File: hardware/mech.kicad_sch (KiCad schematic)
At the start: 16 parts

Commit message: usb, charger, sensors, heir
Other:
- company: (none) -> Frisius
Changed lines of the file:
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@@
 (kicad_sch (version 20211123) (generator eeschema)
-  (paper "A5")
+  (paper "A4")
+  (title_block
+    (company "Frisius")
+  )
   (wire (pts (xy 104.14 45.72) (xy 104.14 44.45))
     (stroke (width 0) (type default) (color 0 0 0 0))

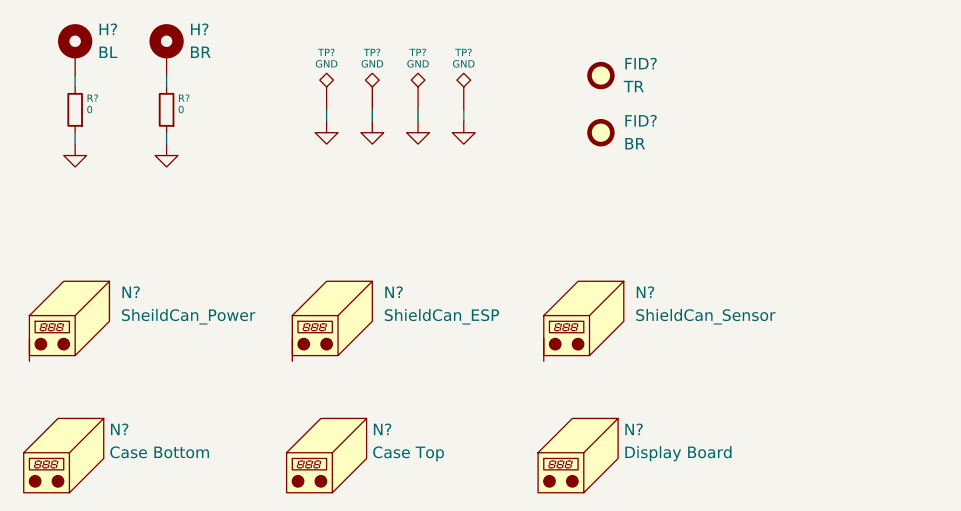
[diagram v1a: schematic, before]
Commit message: checking footprint assignment, added current sense pac1934 for dev
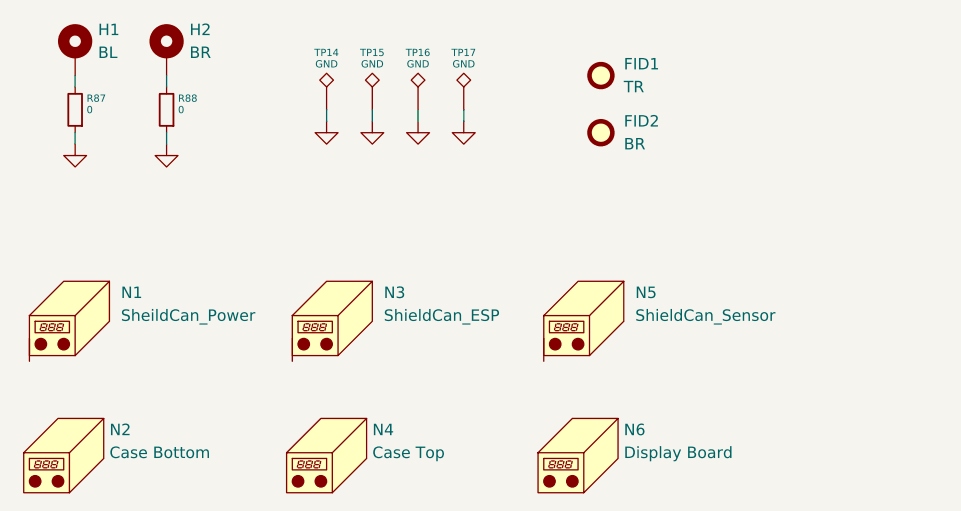
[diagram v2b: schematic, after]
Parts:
- FID1, FID2: renamed from FID?; footprint (none) -> Fiducial:Fiducial_0.5mm_Mask1.5mm
- gave numbers to parts that had none: 14
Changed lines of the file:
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@@
   (symbol (lib_id "power:GND") (at 104.14 45.72 0) (unit 1)
     (in_bom yes) (on_board yes) (fields_autoplaced)
-    (property "Reference" "#PWR?" (id 0) (at 104.14 52.07 0)
+    (property "Reference" "#PWR074" (id 0) (at 104.14 52.07 0)
       (effects (font (size 0.8 0.8)) hide)
     )
@@
   (symbol (lib_id "Mechanical:Housing") (at 128.27 82.55 0) (unit 1)
     (in_bom yes) (on_board yes)
-    (property "Reference" "N?" (id 0) (at 132.08 80.01 0)
+    (property "Reference" "N6" (id 0) (at 132.08 80.01 0)
       (effects (font (size 1.27 1.27)) (justify left))
     )
@@
   (symbol (lib_id "Connector:TestPoint_Alt") (at 114.3 44.45 0) (unit 1)
     (in_bom yes) (on_board yes)
-    (property "Reference" "TP?" (id 0) (at 114.3 38.1 0)
+    (property "Reference" "TP17" (id 0) (at 114.3 38.1 0)
       (effects (font (size 0.8 0.8)))
     )
@@
   (symbol (lib_id "Device:R_Small") (at 81.28 44.45 180) (unit 1)
     (in_bom yes) (on_board yes)
-    (property "Reference" "R?" (id 0) (at 82.55 43.18 0)
+    (property "Reference" "R88" (id 0) (at 82.55 43.18 0)
       (effects (font (size 0.8 0.8)) (justify right))
     )
@@
   (symbol (lib_id "Mechanical:Housing") (at 71.12 82.55 0) (unit 1)
     (in_bom yes) (on_board yes)
-    (property "Reference" "N?" (id 0) (at 74.93 80.01 0)
+    (property "Reference" "N2" (id 0) (at 74.93 80.01 0)
       (effects (font (size 1.27 1.27)) (justify left))
     )
@@
   (symbol (lib_id "power:GND") (at 109.22 45.72 0) (unit 1)
     (in_bom yes) (on_board yes) (fields_autoplaced)
-    (property "Reference" "#PWR?" (id 0) (at 109.22 52.07 0)
+    (property "Reference" "#PWR075" (id 0) (at 109.22 52.07 0)
       (effects (font (size 0.8 0.8)) hide)
     )
@@
   (symbol (lib_id "power:GND") (at 99.06 45.72 0) (unit 1)
     (in_bom yes) (on_board yes) (fields_autoplaced)
-    (property "Reference" "#PWR?" (id 0) (at 99.06 52.07 0)
+    (property "Reference" "#PWR073" (id 0) (at 99.06 52.07 0)
       (effects (font (size 0.8 0.8)) hide)
     )
@@
   (symbol (lib_id "Mechanical:Fiducial") (at 129.54 40.64 0) (unit 1)
     (in_bom yes) (on_board yes) (fields_autoplaced)
-    (property "Reference" "FID?" (id 0) (at 132.08 39.3699 0)
+    (property "Reference" "FID1" (id 0) (at 132.08 39.3699 0)
       (effects (font (size 1.27 1.27)) (justify left))
     )
@@
       (effects (font (size 1.27 1.27)) (justify left))
     )
-    (property "Footprint" "" (id 2) (at 129.54 40.64 0)
+    (property "Footprint" "Fiducial:Fiducial_0.5mm_Mask1.5mm" (id 2) (at 129.54 40.64 0)
       (effects (font (size 1.27 1.27)) hide)
     )
@@
   (symbol (lib_id "Mechanical:Housing_Pad") (at 128.27 67.31 0) (unit 1)
     (in_bom yes) (on_board yes)
-    (property "Reference" "N?" (id 0) (at 133.35 64.77 0)
+    (property "Reference" "N5" (id 0) (at 133.35 64.77 0)
       (effects (font (size 1.27 1.27)) (justify left))
     )
@@
   (symbol (lib_id "Mechanical:Housing") (at 100.33 82.55 0) (unit 1)
     (in_bom yes) (on_board yes)
-    (property "Reference" "N?" (id 0) (at 104.14 80.01 0)
+    (property "Reference" "N4" (id 0) (at 104.14 80.01 0)
       (effects (font (size 1.27 1.27)) (justify left))
     )
@@
   (symbol (lib_id "Mechanical:Housing_Pad") (at 100.33 67.31 0) (unit 1)
     (in_bom yes) (on_board yes)
-    (property "Reference" "N?" (id 0) (at 105.41 64.77 0)
+    (property "Reference" "N3" (id 0) (at 105.41 64.77 0)
       (effects (font (size 1.27 1.27)) (justify left))
     )
@@
   (symbol (lib_id "power:GND") (at 81.28 48.26 0) (unit 1)
     (in_bom yes) (on_board yes) (fields_autoplaced)
-    (property "Reference" "#PWR?" (id 0) (at 81.28 54.61 0)
+    (property "Reference" "#PWR072" (id 0) (at 81.28 54.61 0)
       (effects (font (size 0.8 0.8)) hide)
     )
@@
   (symbol (lib_id "Connector:TestPoint_Alt") (at 104.14 44.45 0) (unit 1)
     (in_bom yes) (on_board yes)
-    (property "Reference" "TP?" (id 0) (at 104.14 38.1 0)
+    (property "Reference" "TP15" (id 0) (at 104.14 38.1 0)
       (effects (font (size 0.8 0.8)))
     )
@@
   (symbol (lib_id "power:GND") (at 71.12 48.26 0) (unit 1)
     (in_bom yes) (on_board yes) (fields_autoplaced)
-    (property "Reference" "#PWR?" (id 0) (at 71.12 54.61 0)
+    (property "Reference" "#PWR071" (id 0) (at 71.12 54.61 0)
       (effects (font (size 0.8 0.8)) hide)
     )
@@
   (symbol (lib_id "Mechanical:Housing_Pad") (at 71.12 67.31 0) (unit 1)
     (in_bom yes) (on_board yes)
-    (property "Reference" "N?" (id 0) (at 76.2 64.77 0)
+    (property "Reference" "N1" (id 0) (at 76.2 64.77 0)
       (effects (font (size 1.27 1.27)) (justify left))
     )
@@
   (symbol (lib_id "Mechanical:MountingHole_Pad") (at 81.28 38.1 0) (unit 1)
     (in_bom yes) (on_board yes) (fields_autoplaced)
-    (property "Reference" "H?" (id 0) (at 83.82 35.5599 0)
+    (property "Reference" "H2" (id 0) (at 83.82 35.5599 0)
       (effects (font (size 1.27 1.27)) (justify left))
     )
@@
   (symbol (lib_id "Mechanical:MountingHole_Pad") (at 71.12 38.1 0) (unit 1)
     (in_bom yes) (on_board yes) (fields_autoplaced)
-    (property "Reference" "H?" (id 0) (at 73.66 35.5599 0)
+    (property "Reference" "H1" (id 0) (at 73.66 35.5599 0)
       (effects (font (size 1.27 1.27)) (justify left))
     )
@@
   (symbol (lib_id "power:GND") (at 114.3 45.72 0) (unit 1)
     (in_bom yes) (on_board yes) (fields_autoplaced)
-    (property "Reference" "#PWR?" (id 0) (at 114.3 52.07 0)
+    (property "Reference" "#PWR076" (id 0) (at 114.3 52.07 0)
       (effects (font (size 0.8 0.8)) hide)
     )
@@
   (symbol (lib_id "Connector:TestPoint_Alt") (at 99.06 44.45 0) (unit 1)
     (in_bom yes) (on_board yes)
-    (property "Reference" "TP?" (id 0) (at 99.06 38.1 0)
+    (property "Reference" "TP14" (id 0) (at 99.06 38.1 0)
       (effects (font (size 0.8 0.8)))
     )
@@
   (symbol (lib_id "Device:R_Small") (at 71.12 44.45 180) (unit 1)
     (in_bom yes) (on_board yes)
-    (property "Reference" "R?" (id 0) (at 72.39 43.18 0)
+    (property "Reference" "R87" (id 0) (at 72.39 43.18 0)
       (effects (font (size 0.8 0.8)) (justify right))
     )
@@
   (symbol (lib_id "Mechanical:Fiducial") (at 129.54 46.99 0) (unit 1)
     (in_bom yes) (on_board yes) (fields_autoplaced)
-    (property "Reference" "FID?" (id 0) (at 132.08 45.7199 0)
+    (property "Reference" "FID2" (id 0) (at 132.08 45.7199 0)
       (effects (font (size 1.27 1.27)) (justify left))
     )
@@
       (effects (font (size 1.27 1.27)) (justify left))
     )
-    (property "Footprint" "" (id 2) (at 129.54 46.99 0)
+    (property "Footprint" "Fiducial:Fiducial_0.5mm_Mask1.5mm" (id 2) (at 129.54 46.99 0)
       (effects (font (size 1.27 1.27)) hide)
     )
@@
   (symbol (lib_id "Connector:TestPoint_Alt") (at 109.22 44.45 0) (unit 1)
     (in_bom yes) (on_board yes)
-    (property "Reference" "TP?" (id 0) (at 109.22 38.1 0)
-      (effects (font (size 0.8 0.8)))
-    )
+    (property "Reference" "TP16" (id 0) (at 109.22 38.1 0)
+      (effects (font (size 0.8 0.8)))
+    )

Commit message: hardware update
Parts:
- removed FID1: TR, Fiducial:Fiducial_0.5mm_Mask1.5mm, symbol Mechanical:Fiducial
- removed FID2: BR, Fiducial:Fiducial_0.5mm_Mask1.5mm, symbol Mechanical:Fiducial
- removed R87, R88: 0, Resistor_SMD:R_0603_1608Metric, symbol Device:R_Small
- removed TP14, TP15, TP16, TP17: GND, TestPoint:TestPoint_Keystone_5015_Micro-Minature, symbol Connector:TestPoint_Alt
- added N7: Battery, symbol Mechanical:Housing
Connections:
- net GND: now also H1.1, H2.1
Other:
- moved on the sheet: H1, H2

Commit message: schematic tidy up, component placement, shielding investigation
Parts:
- removed N5: ShieldCan_Sensor, symbol Mechanical:Housing_Pad
- N3: footprint (none) -> RF_Shielding:Laird_Technologies_BMI-S-102_16.50x16.50mm
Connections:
- net GND: now also N3.1 (PAD)
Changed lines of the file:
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@@
+    (stroke (width 0) (type default) (color 0 0 0 0))
+  )
+  (wire (pts (xy 95.25 73.66) (xy 95.25 72.39))
     (stroke (width 0) (type default) (color 0 0 0 0))
   )
@@
     )
   )
+  (symbol (lib_id "power:GND") (at 95.25 73.66 0) (unit 1)
+    (in_bom yes) (on_board yes) (fields_autoplaced)
+    (property "Reference" "#PWR?" (id 0) (at 95.25 80.01 0)
+      (effects (font (size 0.8 0.8)) hide)
+    )
+    (property "Value" "GND" (id 1) (at 95.25 78.74 0)
+      (effects (font (size 0.8 0.8)) hide)
+    )
+    (property "Footprint" "" (id 2) (at 95.25 73.66 0)
+      (effects (font (size 0.8 0.8)) hide)
+    )
+    (property "Datasheet" "" (id 3) (at 95.25 73.66 0)
+      (effects (font (size 0.8 0.8)) hide)
+    )
+    (pin "1")
+  )
   (symbol (lib_id "Mechanical:Housing") (at 154.94 82.55 0) (unit 1)
     (in_bom yes) (on_board yes)
@@
       (effects (font (size 1.27 1.27)) hide)
     )
-  )
-  (symbol (lib_id "Mechanical:Housing_Pad") (at 128.27 67.31 0) (unit 1)
-    (in_bom yes) (on_board yes)
-    (property "Reference" "N5" (id 0) (at 133.35 64.77 0)
-      (effects (font (size 1.27 1.27)) (justify left))
-    )
-    (property "Value" "ShieldCan_Sensor" (id 1) (at 133.35 67.31 0)
-      (effects (font (size 1.27 1.27)) (justify left))
-    )
-    (property "Footprint" "" (id 2) (at 130.175 66.04 0)
-      (effects (font (size 1.27 1.27)) hide)
-    )
-    (property "Datasheet" "~" (id 3) (at 130.175 66.04 0)
-      (effects (font (size 1.27 1.27)) hide)
-    )
-    (pin "1")
   )
   (symbol (lib_id "Mechanical:Housing") (at 100.33 82.55 0) (unit 1)
@@
       (effects (font (size 1.27 1.27)) (justify left))
     )
-    (property "Footprint" "" (id 2) (at 102.235 66.04 0)
+    (property "Footprint" "RF_Shielding:Laird_Technologies_BMI-S-102_16.50x16.50mm" (id 2) (at 102.235 66.04 0)
       (effects (font (size 1.27 1.27)) hide)
     )

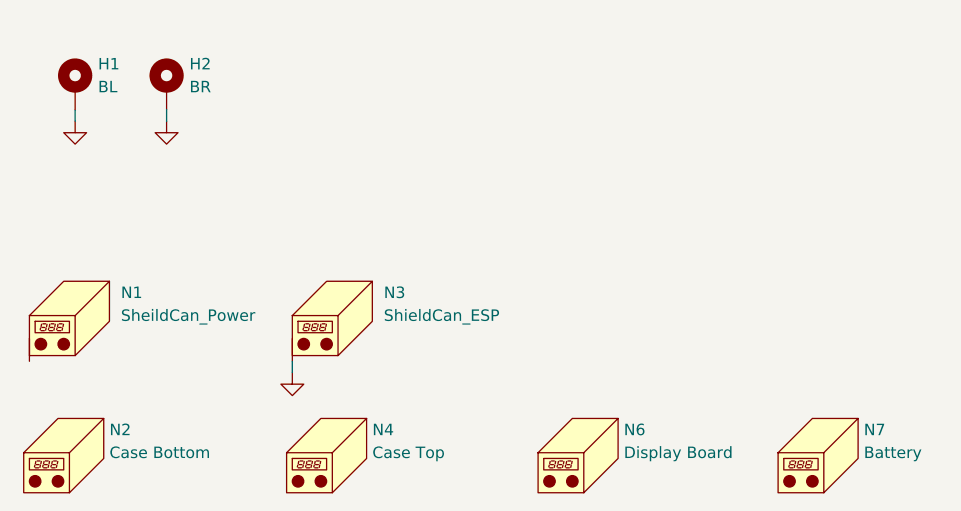
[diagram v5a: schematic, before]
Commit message: minor sch tweaks, more layout, added power emc shield
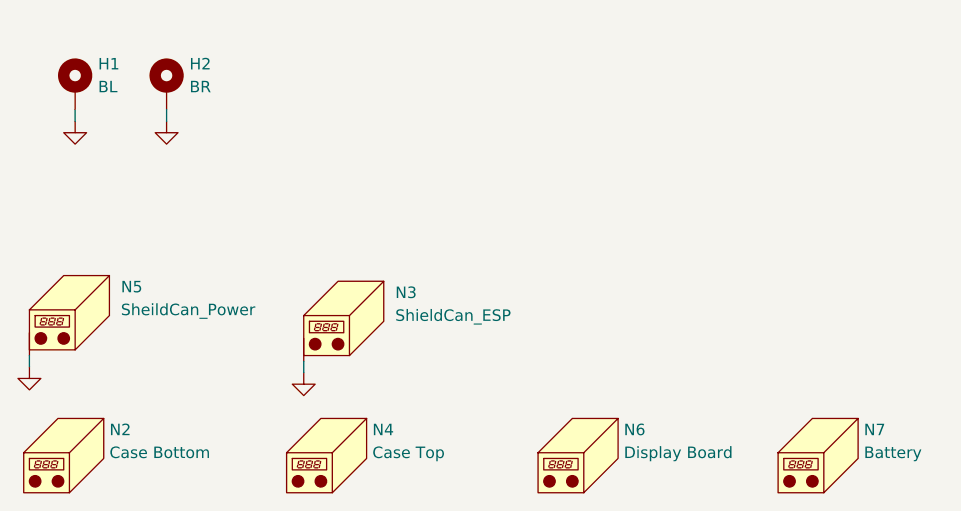
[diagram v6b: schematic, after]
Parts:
- removed N1: SheildCan_Power, symbol Mechanical:Housing_Pad
- added N5: SheildCan_Power, RF_Shielding:Wuerth_36103205_20x20mm, symbol Mechanical:Housing_Pad
- N3: footprint RF_Shielding:Laird_Technologies_BMI-S-102_16.50x16.50mm -> RF_Shielding:Laird_Technologies_BMI-S-101_13.66x12.70mm
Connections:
- net GND: now also N5.1 (PAD)
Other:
- moved on the sheet: N3
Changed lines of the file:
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@@
     (stroke (width 0) (type default) (color 0 0 0 0))
   )
-  (wire (pts (xy 95.25 73.66) (xy 95.25 72.39))
+  (wire (pts (xy 96.52 73.66) (xy 96.52 72.39))
+    (stroke (width 0) (type default) (color 0 0 0 0))
+  )
+  (wire (pts (xy 66.04 73.025) (xy 66.04 71.755))
     (stroke (width 0) (type default) (color 0 0 0 0))
   )
@@
     )
   )
-  (symbol (lib_id "power:GND") (at 95.25 73.66 0) (unit 1)
+  (symbol (lib_id "power:GND") (at 96.52 73.66 0) (unit 1)
     (in_bom yes) (on_board yes) (fields_autoplaced)
-    (property "Reference" "#PWR?" (id 0) (at 95.25 80.01 0)
+    (property "Reference" "#PWR0117" (id 0) (at 96.52 80.01 0)
       (effects (font (size 0.8 0.8)) hide)
     )
-    (property "Value" "GND" (id 1) (at 95.25 78.74 0)
+    (property "Value" "GND" (id 1) (at 96.52 78.74 0)
       (effects (font (size 0.8 0.8)) hide)
     )
-    (property "Footprint" "" (id 2) (at 95.25 73.66 0)
+    (property "Footprint" "" (id 2) (at 96.52 73.66 0)
       (effects (font (size 0.8 0.8)) hide)
     )
-    (property "Datasheet" "" (id 3) (at 95.25 73.66 0)
+    (property "Datasheet" "" (id 3) (at 96.52 73.66 0)
       (effects (font (size 0.8 0.8)) hide)
     )
@@
     )
   )
-  (symbol (lib_id "Mechanical:Housing_Pad") (at 100.33 67.31 0) (unit 1)
+  (symbol (lib_id "Mechanical:Housing_Pad") (at 101.6 67.31 0) (unit 1)
     (in_bom yes) (on_board yes)
-    (property "Reference" "N3" (id 0) (at 105.41 64.77 0)
+    (property "Reference" "N3" (id 0) (at 106.68 64.77 0)
       (effects (font (size 1.27 1.27)) (justify left))
     )
-    (property "Value" "ShieldCan_ESP" (id 1) (at 105.41 67.31 0)
+    (property "Value" "ShieldCan_ESP" (id 1) (at 106.68 67.31 0)
       (effects (font (size 1.27 1.27)) (justify left))
     )
-    (property "Footprint" "RF_Shielding:Laird_Technologies_BMI-S-102_16.50x16.50mm" (id 2) (at 102.235 66.04 0)
+    (property "Footprint" "RF_Shielding:Laird_Technologies_BMI-S-101_13.66x12.70mm" (id 2) (at 103.505 66.04 0)
       (effects (font (size 1.27 1.27)) hide)
     )
-    (property "Datasheet" "~" (id 3) (at 102.235 66.04 0)
+    (property "Datasheet" "~" (id 3) (at 103.505 66.04 0)
       (effects (font (size 1.27 1.27)) hide)
     )
@@
     (pin "1")
   )
+  (symbol (lib_id "power:GND") (at 66.04 73.025 0) (unit 1)
+    (in_bom yes) (on_board yes) (fields_autoplaced)
+    (property "Reference" "#PWR0119" (id 0) (at 66.04 79.375 0)
+      (effects (font (size 0.8 0.8)) hide)
+    )
+    (property "Value" "GND" (id 1) (at 66.04 78.105 0)
+      (effects (font (size 0.8 0.8)) hide)
+    )
+    (property "Footprint" "" (id 2) (at 66.04 73.025 0)
+      (effects (font (size 0.8 0.8)) hide)
+    )
+    (property "Datasheet" "" (id 3) (at 66.04 73.025 0)
+      (effects (font (size 0.8 0.8)) hide)
+    )
+    (pin "1")
+  )
   (symbol (lib_id "power:GND") (at 71.12 45.72 0) (unit 1)
     (in_bom yes) (on_board yes) (fields_autoplaced)
@@
     (property "Datasheet" "" (id 3) (at 71.12 45.72 0)
       (effects (font (size 0.8 0.8)) hide)
-    )
-    (pin "1")
-  )
-  (symbol (lib_id "Mechanical:Housing_Pad") (at 71.12 67.31 0) (unit 1)
-    (in_bom yes) (on_board yes)
-    (property "Reference" "N1" (id 0) (at 76.2 64.77 0)
-      (effects (font (size 1.27 1.27)) (justify left))
-    )
-    (property "Value" "SheildCan_Power" (id 1) (at 76.2 67.31 0)
-      (effects (font (size 1.27 1.27)) (justify left))
-    )
-    (property "Footprint" "" (id 2) (at 73.025 66.04 0)
-      (effects (font (size 1.27 1.27)) hide)
-    )
-    (property "Datasheet" "~" (id 3) (at 73.025 66.04 0)
-      (effects (font (size 1.27 1.27)) hide)
     )
     (pin "1")
@@
       (effects (font (size 1.27 1.27)) hide)
     )
+    (pin "1")
+  )
+  (symbol (lib_id "Mechanical:Housing_Pad") (at 71.12 66.675 0) (unit 1)
+    (in_bom yes) (on_board yes)
+    (property "Reference" "N5" (id 0) (at 76.2 64.135 0)
+      (effects (font (size 1.27 1.27)) (justify left))
+    )
+    (property "Value" "SheildCan_Power" (id 1) (at 76.2 66.675 0)
+      (effects (font (size 1.27 1.27)) (justify left))
+    )
+    (property "Footprint" "RF_Shielding:Wuerth_36103205_20x20mm" (id 2) (at 73.025 65.405 0)
+      (effects (font (size 1.27 1.27)) hide)
+    )
+    (property "Datasheet" "~" (id 3) (at 73.025 65.405 0)
+      (effects (font (size 1.27 1.27)) hide)
+    )

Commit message: screen mock, tweaked layout easier powerplane division
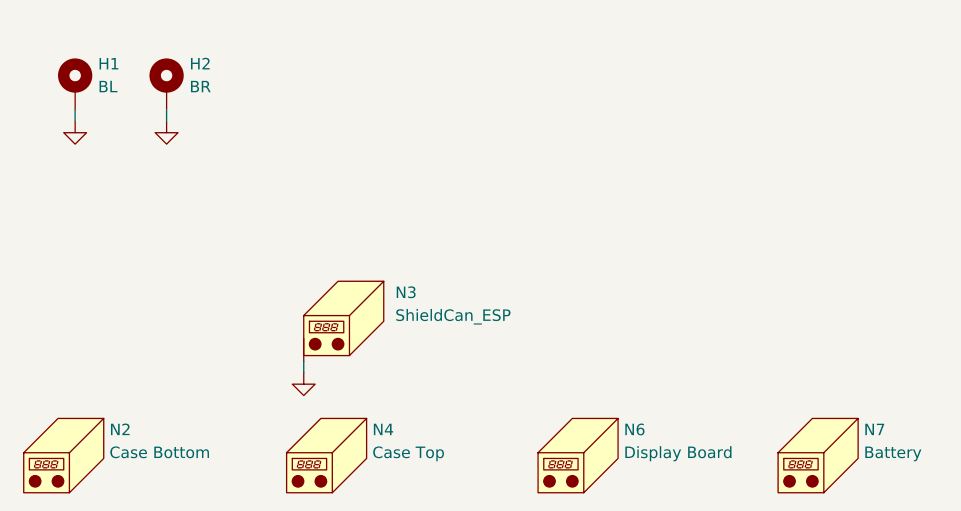
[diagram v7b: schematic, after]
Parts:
- removed N5: SheildCan_Power, RF_Shielding:Wuerth_36103205_20x20mm, symbol Mechanical:Housing_Pad
- N6: footprint (none) -> Fiducial:Fiducial_0.5mm_Mask1.5mm
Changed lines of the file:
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@@
-    (stroke (width 0) (type default) (color 0 0 0 0))
-  )
-  (wire (pts (xy 66.04 73.025) (xy 66.04 71.755))
     (stroke (width 0) (type default) (color 0 0 0 0))
   )
@@
       (effects (font (size 1.27 1.27)) (justify left))
     )
-    (property "Footprint" "" (id 2) (at 129.54 81.28 0)
+    (property "Footprint" "Fiducial:Fiducial_0.5mm_Mask1.5mm" (id 2) (at 129.54 81.28 0)
       (effects (font (size 1.27 1.27)) hide)
     )
@@
     (pin "1")
   )
-  (symbol (lib_id "power:GND") (at 66.04 73.025 0) (unit 1)
-    (in_bom yes) (on_board yes) (fields_autoplaced)
-    (property "Reference" "#PWR0119" (id 0) (at 66.04 79.375 0)
-      (effects (font (size 0.8 0.8)) hide)
-    )
-    (property "Value" "GND" (id 1) (at 66.04 78.105 0)
-      (effects (font (size 0.8 0.8)) hide)
-    )
-    (property "Footprint" "" (id 2) (at 66.04 73.025 0)
-      (effects (font (size 0.8 0.8)) hide)
-    )
-    (property "Datasheet" "" (id 3) (at 66.04 73.025 0)
-      (effects (font (size 0.8 0.8)) hide)
-    )
-    (pin "1")
-  )
   (symbol (lib_id "power:GND") (at 71.12 45.72 0) (unit 1)
     (in_bom yes) (on_board yes) (fields_autoplaced)
@@
       (effects (font (size 1.27 1.27)) hide)
     )
-    (pin "1")
-  )
-  (symbol (lib_id "Mechanical:Housing_Pad") (at 71.12 66.675 0) (unit 1)
-    (in_bom yes) (on_board yes)
-    (property "Reference" "N5" (id 0) (at 76.2 64.135 0)
-      (effects (font (size 1.27 1.27)) (justify left))
-    )
-    (property "Value" "SheildCan_Power" (id 1) (at 76.2 66.675 0)
-      (effects (font (size 1.27 1.27)) (justify left))
-    )
-    (property "Footprint" "RF_Shielding:Wuerth_36103205_20x20mm" (id 2) (at 73.025 65.405 0)
-      (effects (font (size 1.27 1.27)) hide)
-    )
-    (property "Datasheet" "~" (id 3) (at 73.025 65.405 0)
-      (effects (font (size 1.27 1.27)) hide)
-    )
